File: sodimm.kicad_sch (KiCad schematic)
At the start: 3 parts, among them J201 SODIMM-260

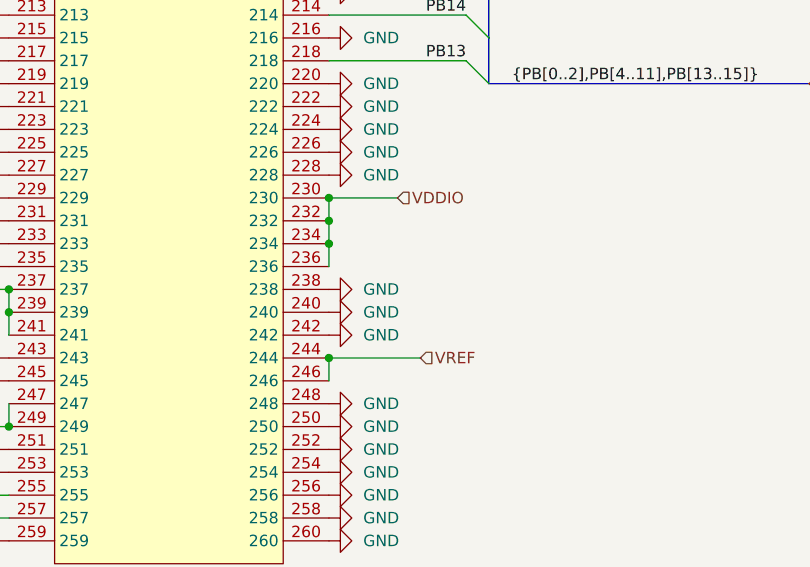
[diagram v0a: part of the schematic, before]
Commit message: small schematic changes, need to reroute
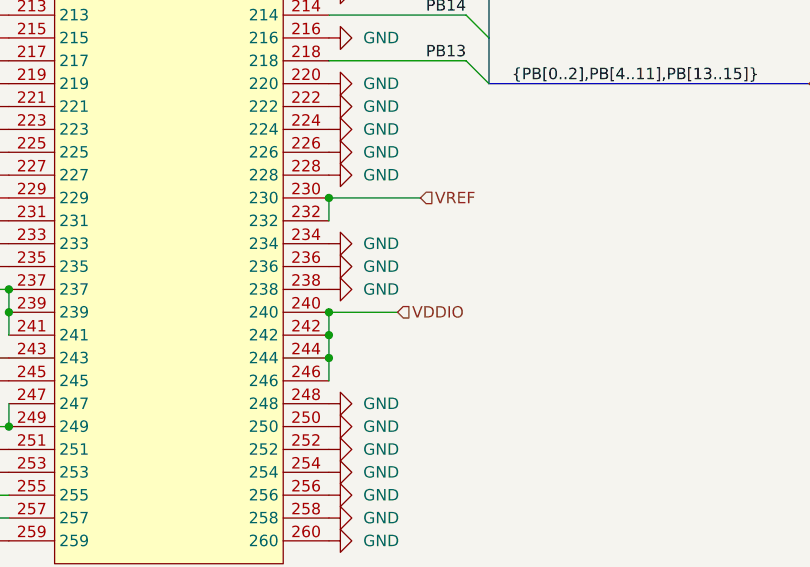
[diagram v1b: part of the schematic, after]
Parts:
- J201: Mating Conector (none) -> https://www.digikey.com/en/products/detail/attend-technolog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
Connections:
- net GND: now also J201.234, J201.236; no longer J201.240, J201.242
- net VDDIO: now also J201.240, J201.242, J201.244, J201.246; no longer J201.230, J201.232, J201.234, J201.236
- net VREF: now also J201.230, J201.232; no longer J201.244, J201.246
